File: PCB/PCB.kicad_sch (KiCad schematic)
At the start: 61 parts, among them J1 USB_C_Receptacle_USB2.0_16P, Q2 IRLML2060, SW1 TSA016A2526B, SW2 TSA016A2526B, SW3 TSA016A2526B, U1 RP2040, U2 USBLC6-2SC6, U3 NCP1117ST33T3G, U4 W25Q32JVSS, U5 Conn, U6 ST25DV04K-JFR6D3, Y1 12MHz

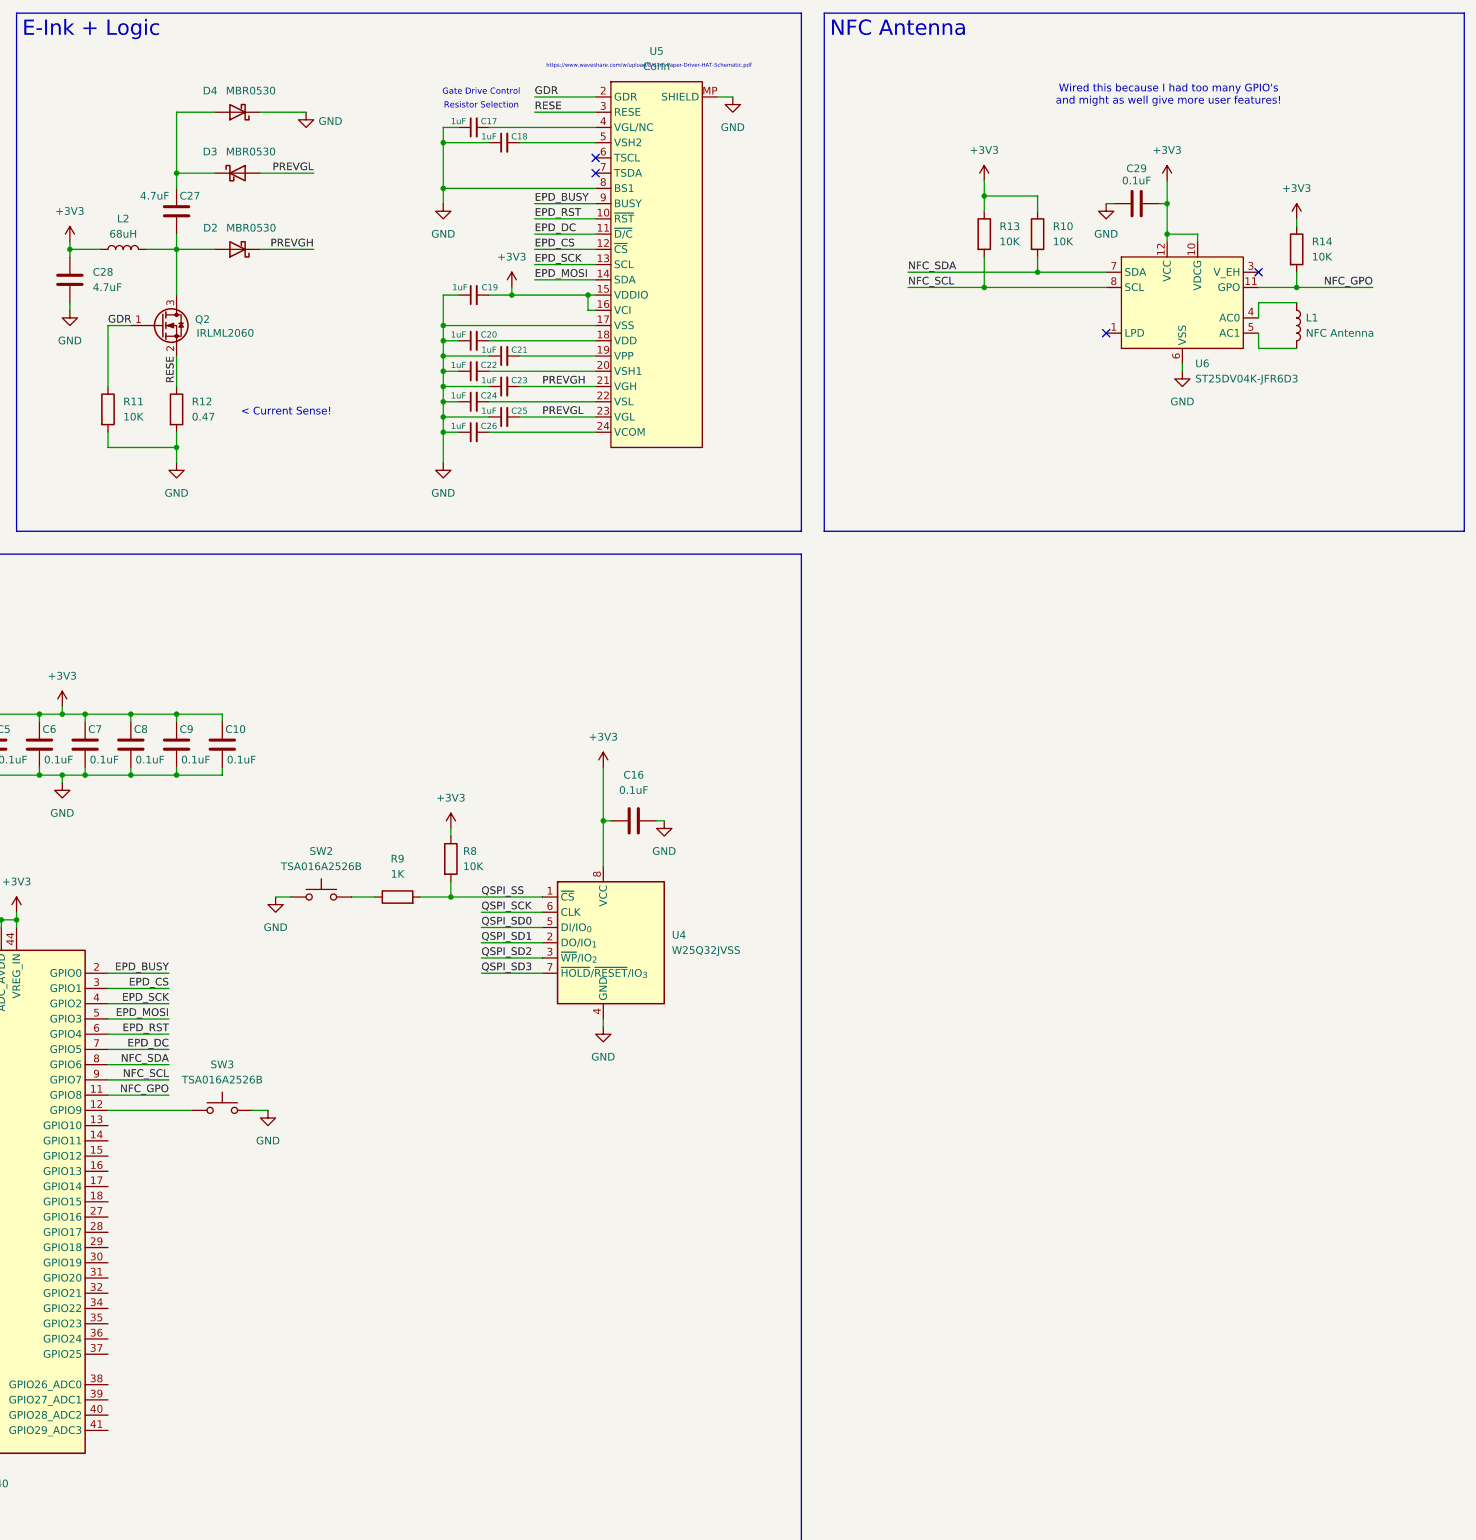
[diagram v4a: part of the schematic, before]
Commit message: cleaned up the schematic and wired MCU pins to get ready for headers
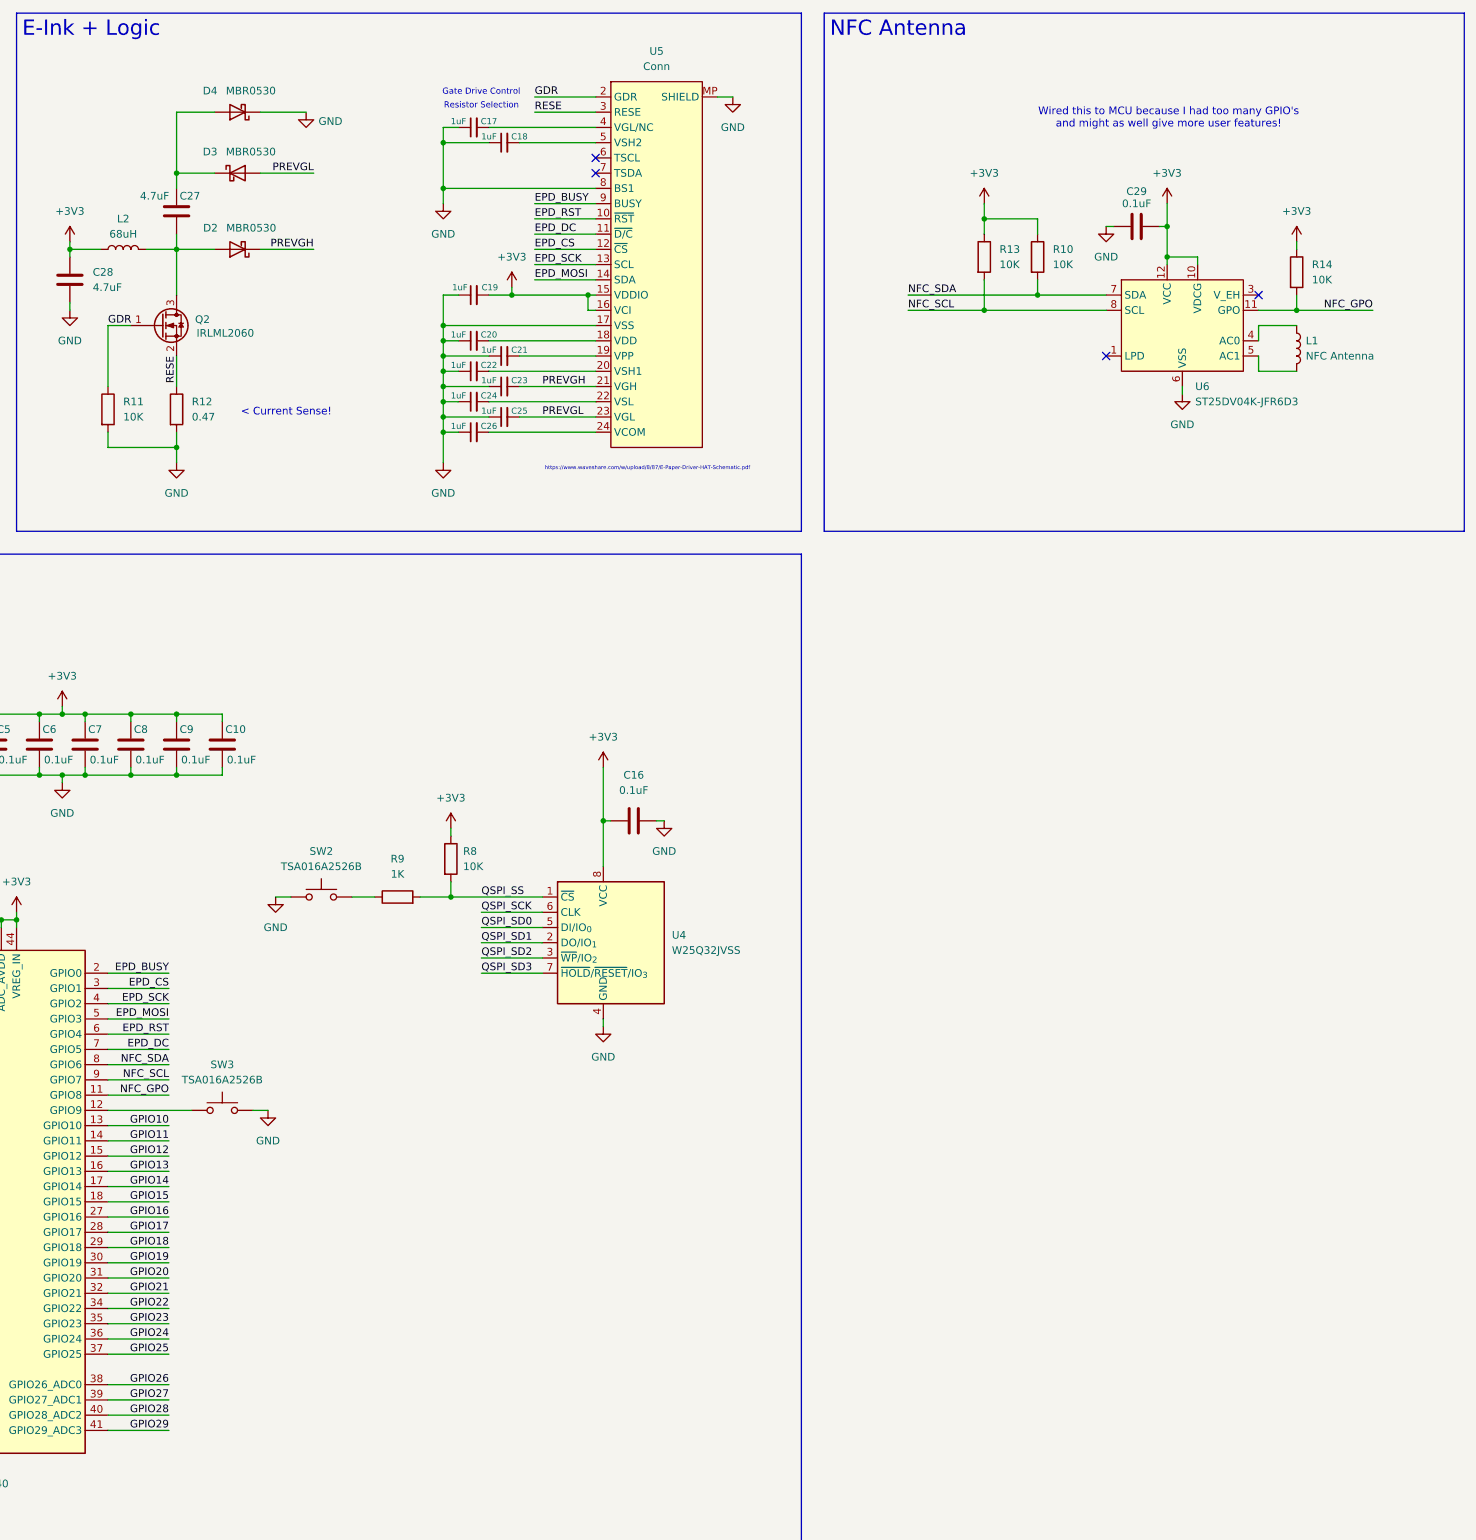
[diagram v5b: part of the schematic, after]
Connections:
- net GPIO10: now reaches U1.13 (GPIO10)
- net GPIO11: now reaches U1.14 (GPIO11)
- net GPIO12: now reaches U1.15 (GPIO12)
- net GPIO13: now reaches U1.16 (GPIO13)
- net GPIO14: now reaches U1.17 (GPIO14)
- net GPIO15: now reaches U1.18 (GPIO15)
- net GPIO16: now reaches U1.27 (GPIO16)
- net GPIO17: now reaches U1.28 (GPIO17)
- net GPIO18: now reaches U1.29 (GPIO18)
- net GPIO19: now reaches U1.30 (GPIO19)
- net GPIO20: now reaches U1.31 (GPIO20)
- net GPIO21: now reaches U1.32 (GPIO21)
- net GPIO22: now reaches U1.34 (GPIO22)
- net GPIO23: now reaches U1.35 (GPIO23)
- net GPIO24: now reaches U1.36 (GPIO24)
- net GPIO25: now reaches U1.37 (GPIO25)
- net GPIO26: now reaches U1.38 (GPIO26_ADC0)
- net GPIO27: now reaches U1.39 (GPIO27_ADC1)
- net GPIO28: now reaches U1.40 (GPIO28_ADC2)
- net GPIO29: now reaches U1.41 (GPIO29_ADC3)
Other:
- note added: "Wired this to MCU because I had too many GPIO's and might as well give more user features!"
- note removed: "Wired this because I had too many GPIO's and might as well give more user features!"
- moved on the sheet: C29, L1, R10, R13, R14, U6

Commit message: added the header pins in!
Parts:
- added J2, J3: Conn_01x15, symbol Connector_Generic:Conn_01x15
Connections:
- net +3V3: now also J2.5 (Pin_5), J3.5 (Pin_5)
- net +5V: now also J2.1 (Pin_1), J3.1 (Pin_1)
- net GND: now also J2.13 (Pin_13), J2.3 (Pin_3), J2.8 (Pin_8), J3.13 (Pin_13), J3.3 (Pin_3), J3.8 (Pin_8)
- net GPIO10: now also J2.2 (Pin_2)
- net GPIO11: now also J2.4 (Pin_4)
- net GPIO12: now also J2.6 (Pin_6)
- net GPIO13: now also J2.7 (Pin_7)
- net GPIO14: now also J2.9 (Pin_9)
- net GPIO15: now also J2.10 (Pin_10)
- net GPIO16: now also J2.11 (Pin_11)
- net GPIO17: now also J2.12 (Pin_12)
- net GPIO18: now also J2.14 (Pin_14)
- net GPIO19: now also J2.15 (Pin_15)
- net GPIO20: now also J3.2 (Pin_2)
- net GPIO21: now also J3.4 (Pin_4)
- net GPIO22: now also J3.6 (Pin_6)
- net GPIO23: now also J3.7 (Pin_7)
- net GPIO24: now also J3.9 (Pin_9)
- net GPIO25: now also J3.10 (Pin_10)
- net GPIO26: now also J3.11 (Pin_11)
- net GPIO27: now also J3.12 (Pin_12)
- net GPIO28: now also J3.14 (Pin_14)
- net GPIO29: now also J3.15 (Pin_15)

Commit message: finishing touches to the schematic
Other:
- note added: "Holes are top/bottom instead of sides!"
- note added: "Made by @KaiPereira :D"
- note added: "Not castellated because of extra costs"
- note added: "Power on each side, because board is wider!"
- moved on the sheet: J2, J3

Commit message: added in my custom header footprint
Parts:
- J2, J3: footprint (none) -> kai's library:PinHeader_PAD_1x15_P2.54mm_Vertical
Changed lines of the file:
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@@
 			)
 		)
-		(property "Footprint" ""
+		(property "Footprint" "kai's library:PinHeader_PAD_1x15_P2.54mm_Vertical"
 			(at 360.68 154.94 0)
 			(effects
@@
 			)
 		)
-		(property "Footprint" ""
+		(property "Footprint" "kai's library:PinHeader_PAD_1x15_P2.54mm_Vertical"
 			(at 337.82 154.94 0)
 			(effects
